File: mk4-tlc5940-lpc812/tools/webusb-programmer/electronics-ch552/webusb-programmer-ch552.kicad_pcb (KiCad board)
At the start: 2 copper layers, 38 x 20 mm, 20 parts, among them J1 Light Controller, J2 USB_B_Micro, Q1 PMV30UN, U1 STMPS2141STR, U2 MCP1703A-3302_SOT23, U3 CH552G

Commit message: Add test points to trigger bootloader
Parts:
- added TP1: , WLA_pinheader:TestPoint_THTPad_1.0x1.0mm_Drill0.5mm_nosilk, F.Cu at (108.3, 102.0)
- added TP2: , WLA_pinheader:TestPoint_THTPad_1.0x1.0mm_Drill0.5mm_nosilk, F.Cu at (108.3, 100.0)
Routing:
- net +3V3: track 30.1 -> 32.4 mm
- net /USB-DP: track 22.7 -> 23.8 mm
- net /USB-DM: track 27.0 -> 27.6 mm

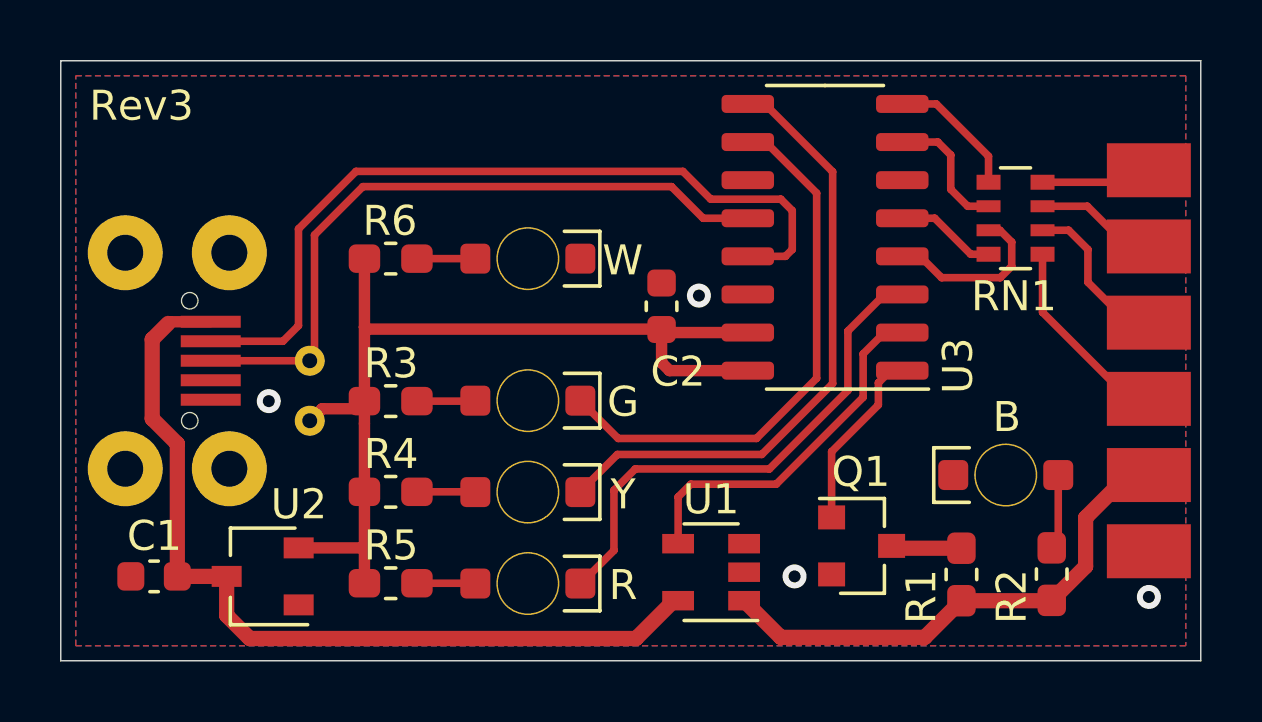
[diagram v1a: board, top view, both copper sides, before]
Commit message: Reduce complexity by using internal LDO and no shorting MOSFET
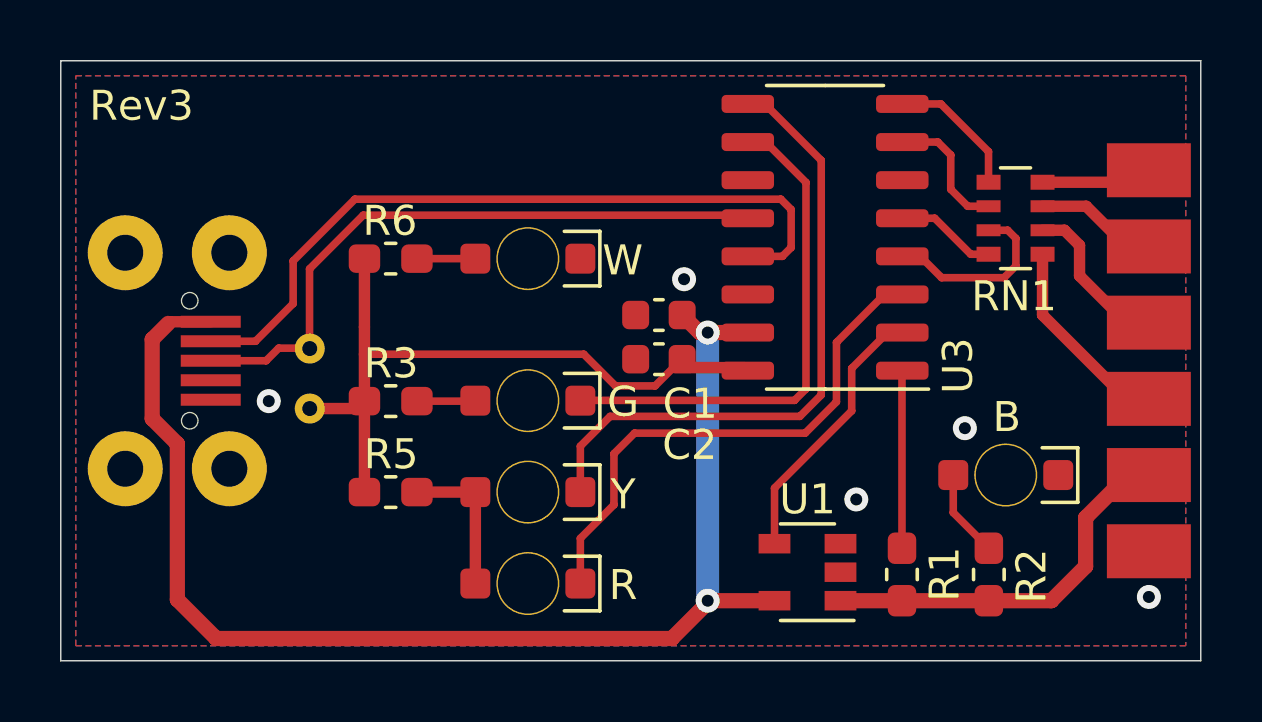
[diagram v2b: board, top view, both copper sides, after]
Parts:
- removed Q1: PMV30UN, Package_TO_SOT_SMD:SOT-23
- removed R4: 1k2, Resistor_SMD:R_0603_1608Metric_Pad1.05x0.95mm_HandSolder
- removed U2: MCP1703A-3302_SOT23, Package_TO_SOT_SMD:SOT-23W
- moved C1 18.9 mm to (119.9, 98.5)
- moved U1 3.21 mm to (124.9, 107.0)
- moved R5 3.04 mm to (111.0, 104.4)
- moved R2 2.10 mm to (130.9, 107.1)
- moved R1 1.98 mm to (128.0, 107.1)
- moved C2 1.77 mm to (119.9, 99.9), turned to 180 degrees
- moved TP1 0.41 mm to (108.3, 101.6)
- moved TP2 0.41 mm to (108.3, 99.6)
- turned D1 to 180 degrees
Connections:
- D4 pad 2: Net-(D4-Pad2) -> Net-(D3-Pad2)
- R1 pad 2: Net-(Q1-Pad3) -> /SHORT
- R5 pad 2: Net-(D4-Pad2) -> Net-(D3-Pad2)
- U3 pad 15: +3V3 -> +5V
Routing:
- net +5V: track 29.3 -> 43.7 mm, vias 0 -> 2
- net +3V3: track 32.4 -> 23.4 mm
- net /VLIGHT: track 17.2 -> 13.0 mm
- net Net-(D3-Pad2): track 1.95 -> 5.01 mm
- net /EN: track 12.1 -> 9.09 mm
- net Net-(Q1-Pad3): track 2.36 -> 0.00 mm
- net Net-(D4-Pad2): track 1.95 -> 0.00 mm
- net /USB-DM: track 27.6 -> 25.7 mm
- net /USB-DP: track 23.8 -> 22.2 mm
- net /OK: track 18.4 -> 17.1 mm
- net /ERROR: track 17.1 -> 17.8 mm
- net /BUSY: track 20.7 -> 21.3 mm
- net GND: vias 4 -> 5
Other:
- board text added: "WebUSB programmer"
- board text removed: "Light Controller WebUSB programmer"

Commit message: Use side-mount LEDs
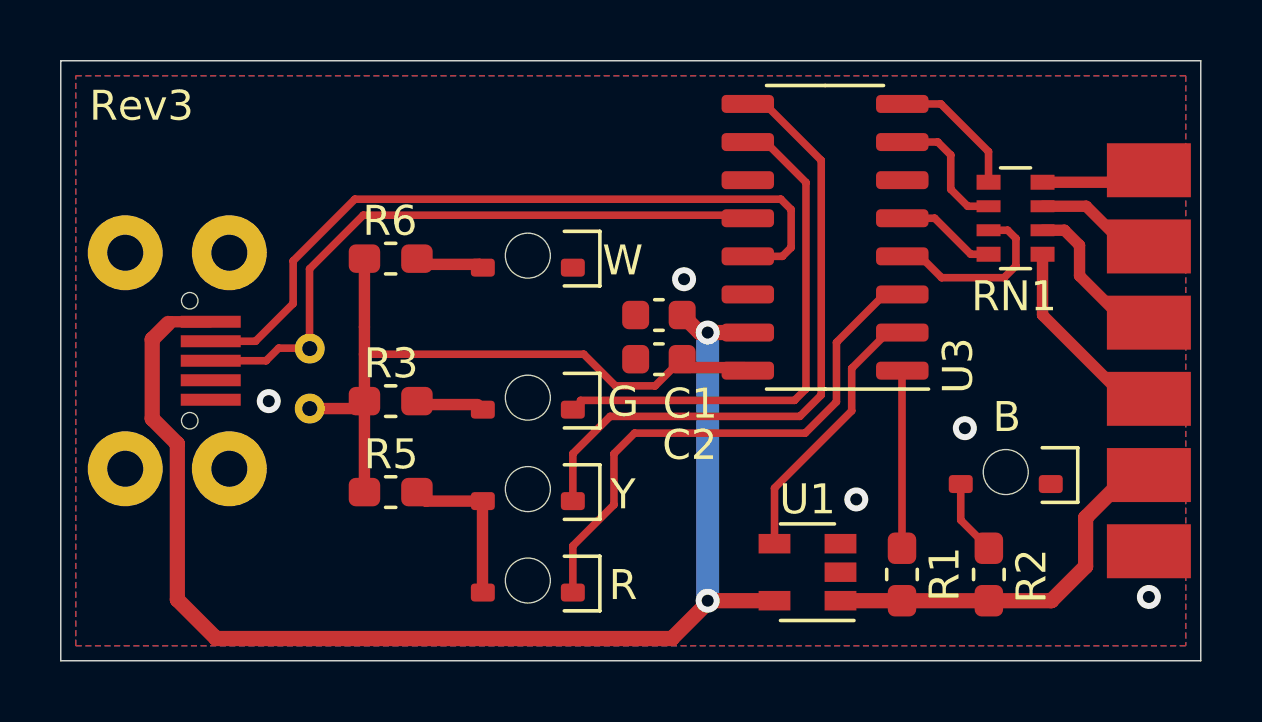
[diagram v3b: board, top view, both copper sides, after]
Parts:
- D1, D2, D3, D4, D5: footprint WLA_LED_reverse_mount:LED_1204_reverse_mout -> WLA_LED_reverse_mount:LED_1204_side_mout
- R1: value 10 -> 100

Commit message: Tweak LED footprint and improve layout
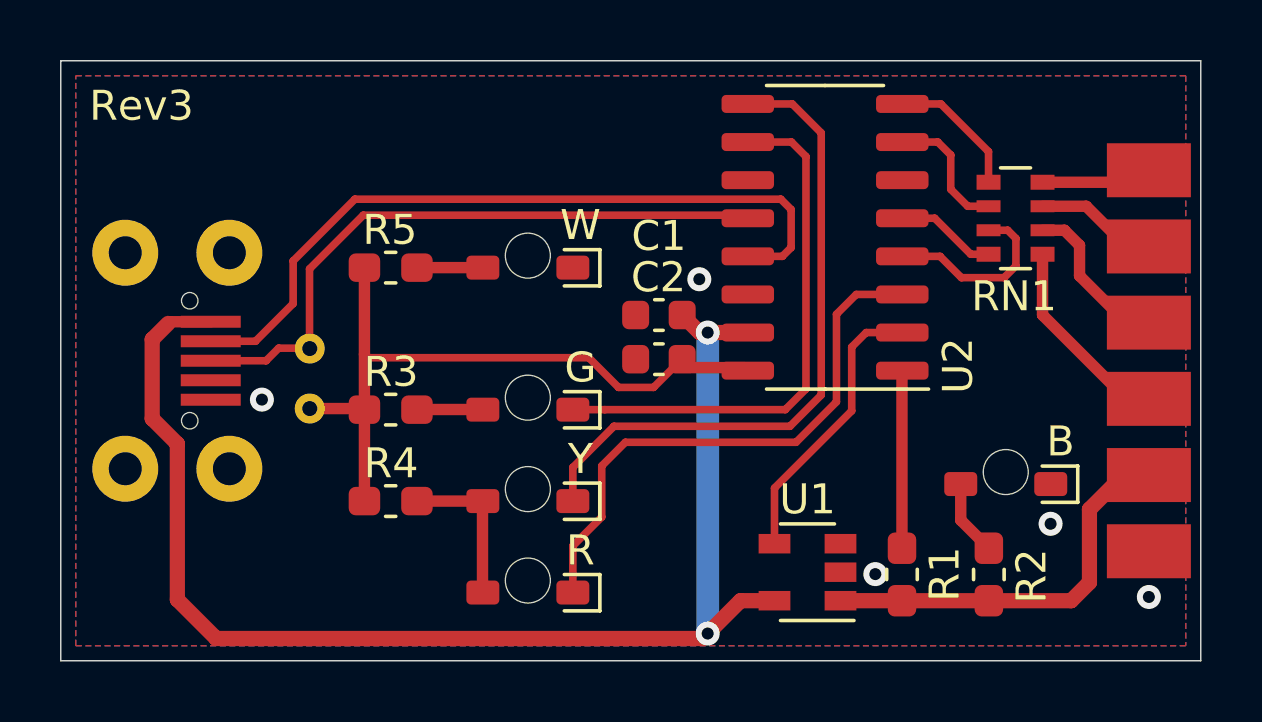
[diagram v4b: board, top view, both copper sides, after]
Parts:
- J2: footprint USB:Mirco_USB_Type_B_LCSC_C40943 -> WLA_USB:Mirco_USB_Type_B_LCSC_C40943
- moved R5 0.30 mm to (111.0, 96.9)
- moved R4 0.30 mm to (111.0, 104.7)
- moved R3 0.28 mm to (111.0, 101.6)
- renumbered R5 to R4, R6 to R5, U3 to U2
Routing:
- net +5V: track 43.7 -> 44.8 mm
- net /OK: track 17.1 -> 18.0 mm
- net /ERROR: track 18.2 -> 18.7 mm

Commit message: Improve USB footprint and layout and silkscreen
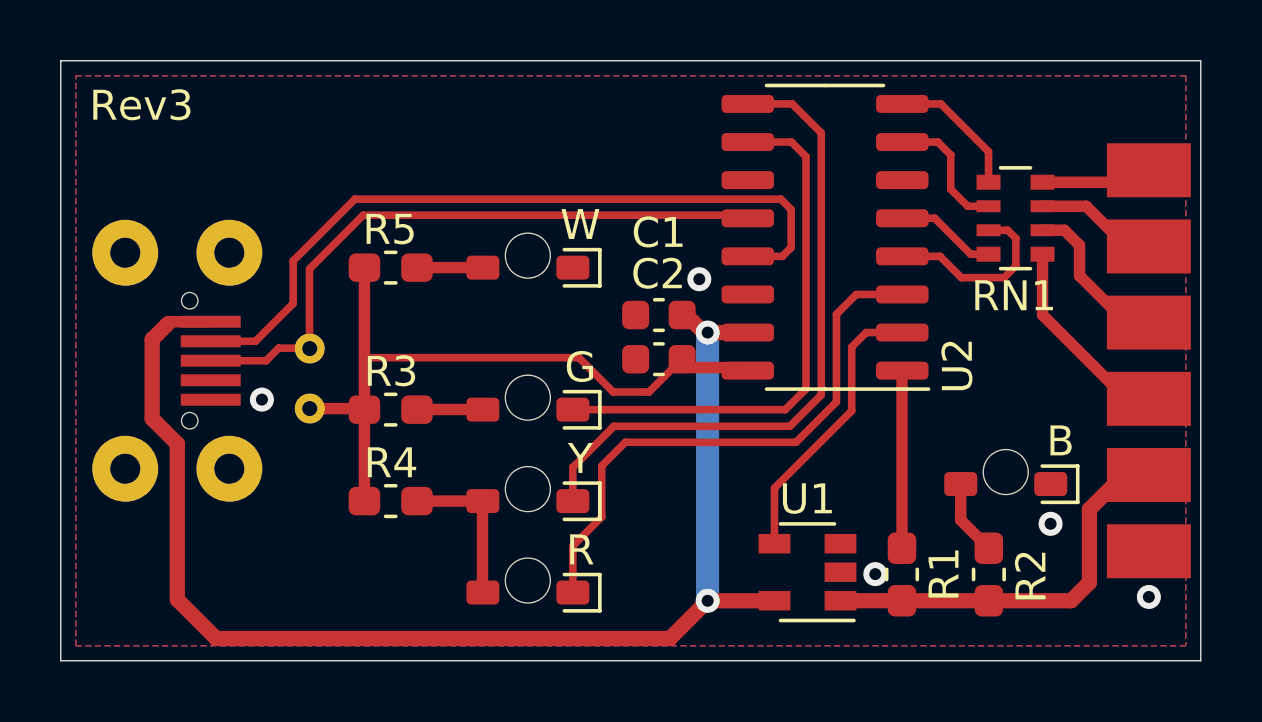
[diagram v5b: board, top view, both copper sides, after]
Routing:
- net +5V: track 44.8 -> 43.7 mm
